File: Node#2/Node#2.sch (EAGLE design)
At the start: 75 parts, among them IC1 TSL25911FN, J1 68712414522, Q2 SI1308EDL-T1-GE3, U2 RV8564C3, U4 TPS63001DRCT

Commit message: Node#2 sorted, Node#1 small adjusts
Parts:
- added R2: 100, rcl:R-EU_R0805
- added U$9: BZB984, BlueHome:BZB984
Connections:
- new net N$2: D2.A, R2.1
- net +3V3: no longer D2.A
- net +3V3_RTC: now also U$9.2
- net GND: now also U$9.3
- net V+: now also R2.2

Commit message: Schematic finished (hopefully) !
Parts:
- added C34: (no value), rcl:C-EUC0805
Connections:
- removed net N$26: C31.2, C33.2, MK1.VDD
- net +3V3: now also MK1.VDD
- net +5V: no longer U$1.2
- net ADC2: now also C34.1
- net GND: now also C31.2, C33.2, C34.2
- net V+: now also U$1.2
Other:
- note added: "E-Ink Display"
- note added: "Power"
- note added: "Sensors & LEDs"

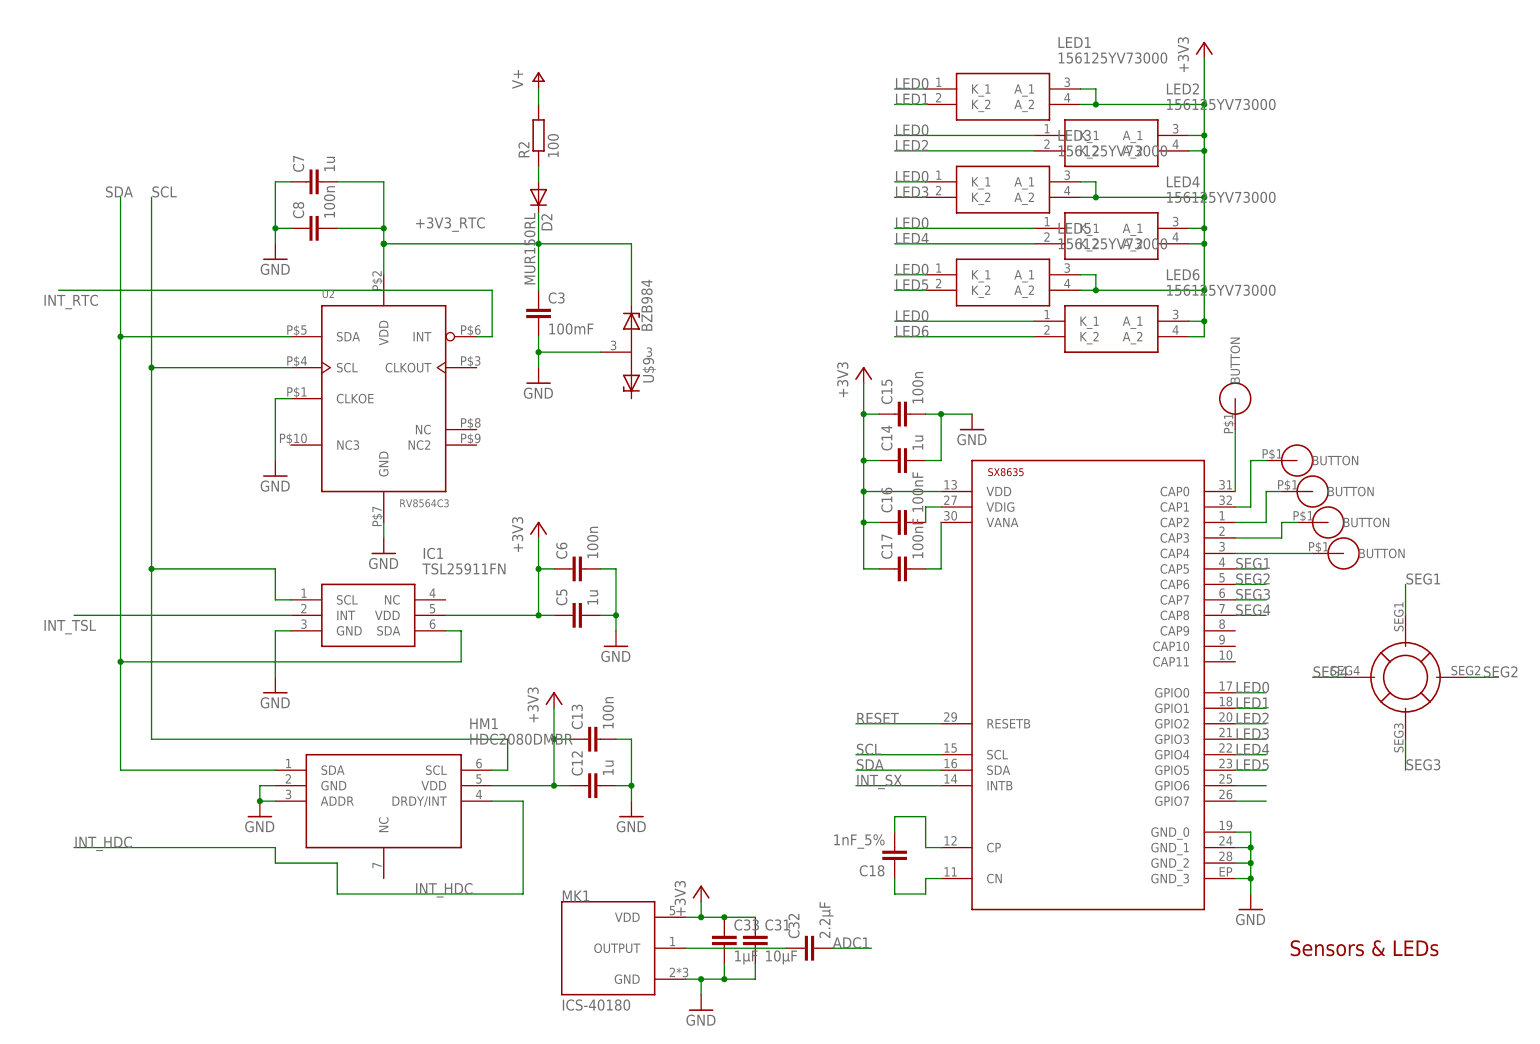
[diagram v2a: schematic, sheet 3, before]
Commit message: Changed Packages, connected GPIO
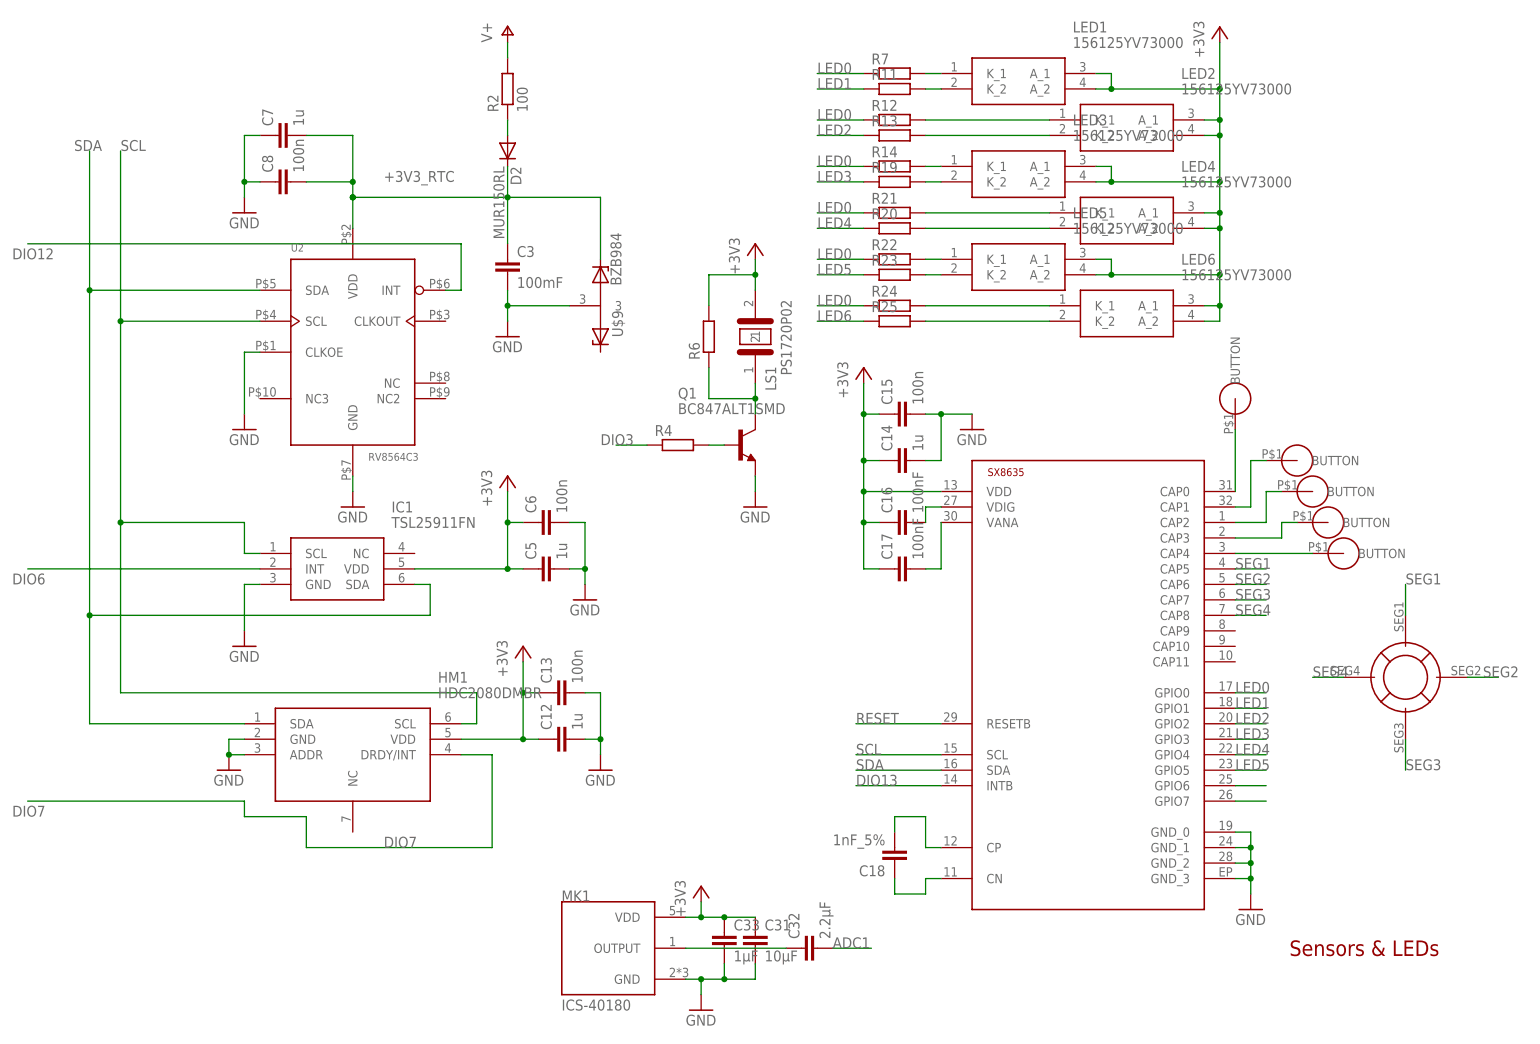
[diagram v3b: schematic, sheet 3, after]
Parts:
- added LS1: PS1720P02, BlueHome:PS1720P02
- added Q1: BC847ALT1SMD, transistor-npn:BC847ALT1SMD
- added R11, R12, R13, R14, R19, R20, R21, R22, R23, R24, R25, R4, R6, R7: (no value), rcl:R-EU_R0805
- L1: device rcl:L-EUL4532P -> rcl:L-EUL5038P
- L2: device rcl:L-EUL1812 -> rcl:L-EUL5038P
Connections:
- net INT_HDC renamed DIO7
- net INT_RTC renamed DIO12
- net INT_SX renamed DIO13
- net INT_TSL renamed DIO6
- new net DIO0: J1.13
- new net DIO1: J1.12
- new net DIO2: J1.14
- new net DIO3: R4.1
- new net N$13: LED3.K_2, R19.2
- new net N$16: LED5.K_1, R22.2
- new net N$17: LED5.K_2, R23.2
- new net N$25: LED2.K_1, R12.2
- new net N$26: LED2.K_2, R13.2
- new net N$27: LED4.K_1, R21.2
- new net N$3: LS1.1, Q1.C, R6.1
- new net N$30: LED4.K_2, R20.2
- new net N$36: LED6.K_1, R24.2
- new net N$37: LED6.K_2, R25.2
- new net N$4: LED1.K_1, R7.2
- new net N$5: LED1.K_2, R11.2
- new net N$6: Q1.B, R4.2
- new net N$7: LED3.K_1, R14.2
- net +3V3: now also LS1.2, R6.2
- net CS: no longer J1.12
- net GND: now also Q1.E
- net LED0: now also R12.1, R14.1, R21.1, R22.1, R24.1, R7.1; no longer LED1.K_1, LED2.K_1, LED3.K_1, LED4.K_1, LED5.K_1, LED6.K_1
- net LED1: now also R11.1; no longer LED1.K_2
- net LED2: now also R13.1; no longer LED2.K_2
- net LED3: now also R19.1; no longer LED3.K_2
- net LED4: now also R20.1; no longer LED4.K_2
- net LED5: now also R23.1; no longer LED5.K_2
- net LED6: now also R25.1; no longer LED6.K_2
- net MOSI: no longer J1.14
- net SCLK: no longer J1.13
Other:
- moved on the sheet: C12, C13, C3, C5, C6, C7, C8, D2, HM1, IC1, LED1, LED2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

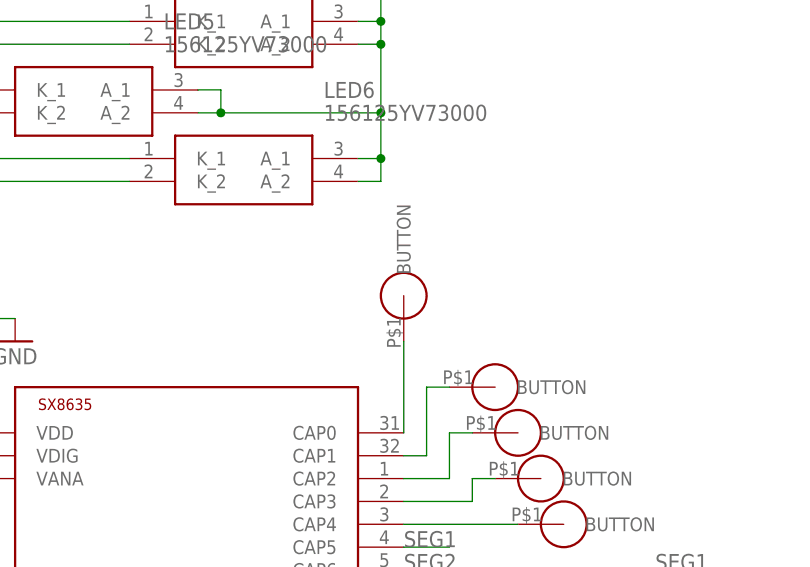
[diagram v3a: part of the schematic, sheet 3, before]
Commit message: Created node#2 Layout and Proximity Sensor in Library
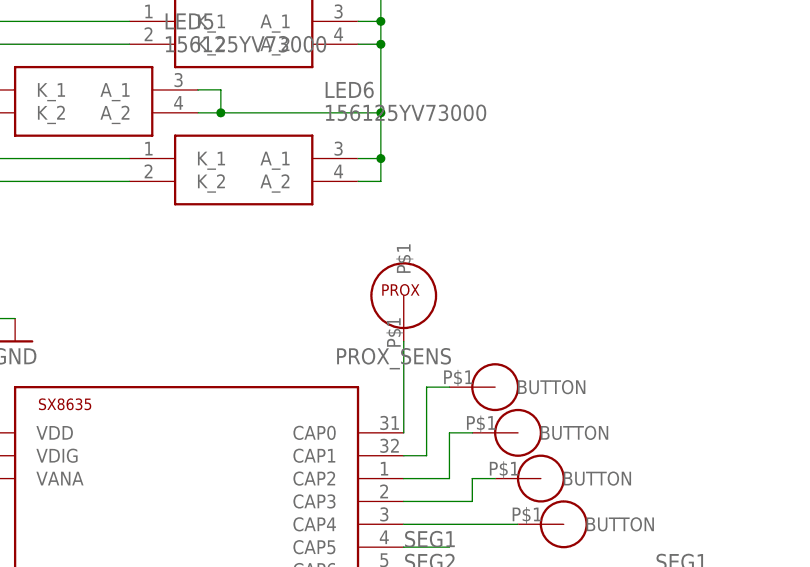
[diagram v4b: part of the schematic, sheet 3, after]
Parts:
- U$7: value TOUCH_BUTTON -> PROXIMITY; device BlueHome:TOUCH_BUTTON -> BlueHome:PROXIMITY
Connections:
- removed net +5V: R5.2
- removed net N$33: U$2.CAP0, U$7.BUTTON
- new net PROX_SENS: U$2.CAP0, U$7.P$1
- net V+: now also R5.2
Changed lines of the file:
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@@
 <grid distance="0.1" unitdist="inch" unit="inch" style="lines" multiple="1" display="no" altdistance="0.01" altunitdist="inch" altunit="inch"/>
 <layers>
-<layer number="1" name="Top" color="4" fill="1" visible="yes" active="no"/>
-<layer number="2" name="Route2" color="1" fill="3" visible="yes" active="no"/>
-<layer number="3" name="Route3" color="4" fill="3" visible="yes" active="no"/>
-<layer number="4" name="Route4" color="1" fill="4" visible="yes" active="no"/>
-<layer number="5" name="Route5" color="4" fill="4" visible="yes" active="no"/>
-<layer number="6" name="Route6" color="1" fill="8" visible="yes" active="no"/>
-<layer number="7" name="Route7" color="4" fill="8" visible="yes" active="no"/>
-<layer number="8" name="Route8" color="1" fill="2" visible="yes" active="no"/>
-<layer number="9" name="Route9" color="4" fill="2" visible="yes" active="no"/>
-<layer number="10" name="Route10" color="1" fill="7" visible="yes" active="no"/>
-<layer number="11" name="Route11" color="4" fill="7" visible="yes" active="no"/>
-<layer number="12" name="Route12" color="1" fill="5" visible="yes" active="no"/>
-<layer number="13" name="Route13" color="4" fill="5" visible="yes" active="no"/>
-<layer number="14" name="Route14" color="1" fill="6" visible="yes" active="no"/>
-<layer number="15" name="Route15" color="4" fill="6" visible="yes" active="no"/>
-<layer number="16" name="Bottom" color="1" fill="1" visible="yes" active="no"/>
-<layer number="17" name="Pads" color="2" fill="1" visible="yes" active="no"/>
-<layer number="18" name="Vias" color="2" fill="1" visible="yes" active="no"/>
-<layer number="19" name="Unrouted" color="6" fill="1" visible="yes" active="no"/>
-<layer number="20" name="Dimension" color="15" fill="1" visible="yes" active="no"/>
-<layer number="21" name="tPlace" color="7" fill="1" visible="yes" active="no"/>
-<layer number="22" name="bPlace" color="7" fill="1" visible="yes" active="no"/>
-<layer number="23" name="tOrigins" color="15" fill="1" visible="yes" active="no"/>
-<layer number="24" name="bOrigins" color="15" fill="1" visible="yes" active="no"/>
-<layer number="25" name="tNames" color="7" fill="1" visible="yes" active="no"/>
-<layer number="26" name="bNames" color="7" fill="1" visible="yes" active="no"/>
-<layer number="27" name="tValues" color="7" fill="1" visible="yes" active="no"/>
-<layer number="28" name="bValues" color="7" fill="1" visible="yes" active="no"/>
+<layer number="1" name="Top" color="4" fill="1" visible="no" active="no"/>
+<layer number="2" name="Route2" color="1" fill="3" visible="no" active="no"/>
+<layer number="3" name="Route3" color="4" fill="3" visible="no" active="no"/>
+<layer number="4" name="Route4" color="1" fill="4" visible="no" active="no"/>
+<layer number="5" name="Route5" color="4" fill="4" visible="no" active="no"/>
+<layer number="6" name="Route6" color="1" fill="8" visible="no" active="no"/>
+<layer number="7" name="Route7" color="4" fill="8" visible="no" active="no"/>
+<layer number="8" name="Route8" color="1" fill="2" visible="no" active="no"/>
+<layer number="9" name="Route9" color="4" fill="2" visible="no" active="no"/>
+<layer number="10" name="Route10" color="1" fill="7" visible="no" active="no"/>
+<layer number="11" name="Route11" color="4" fill="7" visible="no" active="no"/>
+<layer number="12" name="Route12" color="1" fill="5" visible="no" active="no"/>
+<layer number="13" name="Route13" color="4" fill="5" visible="no" active="no"/>
+<layer number="14" name="Route14" color="1" fill="6" visible="no" active="no"/>
+<layer number="15" name="Route15" color="4" fill="6" visible="no" active="no"/>
+<layer number="16" name="Bottom" color="1" fill="1" visible="no" active="no"/>
+<layer number="17" name="Pads" color="2" fill="1" visible="no" active="no"/>
+<layer number="18" name="Vias" color="2" fill="1" visible="no" active="no"/>
+<layer number="19" name="Unrouted" color="6" fill="1" visible="no" active="no"/>
+<layer number="20" name="Dimension" color="15" fill="1" visible="no" active="no"/>
+<layer number="21" name="tPlace" color="7" fill="1" visible="no" active="no"/>
+<layer number="22" name="bPlace" color="7" fill="1" visible="no" active="no"/>
+<layer number="23" name="tOrigins" color="15" fill="1" visible="no" active="no"/>
+<layer number="24" name="bOrigins" color="15" fill="1" visible="no" active="no"/>
+<layer number="25" name="tNames" color="7" fill="1" visible="no" active="no"/>
+<layer number="26" name="bNames" color="7" fill="1" visible="no" active="no"/>
+<layer number="27" name="tValues" color="7" fill="1" visible="no" active="no"/>
+<layer number="28" name="bValues" color="7" fill="1" visible="no" active="no"/>
 <layer number="29" name="tStop" color="7" fill="3" visible="no" active="no"/>
 <layer number="30" name="bStop" color="7" fill="6" visible="no" active="no"/>
@@
 <layer number="35" name="tGlue" color="7" fill="4" visible="no" active="no"/>
 <layer number="36" name="bGlue" color="7" fill="5" visible="no" active="no"/>
-<layer number="37" name="tTest" color="7" fill="1" visible="yes" active="no"/>
-<layer number="38" name="bTest" color="7" fill="1" visible="yes" active="no"/>
+<layer number="37" name="tTest" color="7" fill="1" visible="no" active="no"/>
+<layer number="38" name="bTest" color="7" fill="1" visible="no" active="no"/>
 <layer number="39" name="tKeepout" color="4" fill="11" visible="no" active="no"/>
 <layer number="40" name="bKeepout" color="1" fill="11" visible="no" active="no"/>
@@
 <layer number="44" name="Drills" color="7" fill="1" visible="no" active="no"/>
 <layer number="45" name="Holes" color="7" fill="1" visible="no" active="no"/>
-<layer number="46" name="Milling" color="3" fill="1" visible="yes" active="no"/>
-<layer number="47" name="Measures" color="7" fill="1" visible="yes" active="no"/>
-<layer number="48" name="Document" color="7" fill="1" visible="yes" active="no"/>
-<layer number="49" name="Reference" color="7" fill="1" visible="yes" active="no"/>
-<layer number="51" name="tDocu" color="7" fill="1" visible="yes" active="no"/>
-<layer number="52" name="bDocu" color="7" fill="1" visible="yes" active="no"/>
+<layer number="46" name="Milling" color="3" fill="1" visible="no" active="no"/>
+<layer number="47" name="Measures" color="7" fill="1" visible="no" active="no"/>
+<layer number="48" name="Document" color="7" fill="1" visible="no" active="no"/>
+<layer number="49" name="Reference" color="7" fill="1" visible="no" active="no"/>
+<layer number="51" name="tDocu" color="7" fill="1" visible="no" active="no"/>
+<layer number="52" name="bDocu" color="7" fill="1" visible="no" active="no"/>
 <layer number="90" name="Modules" color="5" fill="1" visible="yes" active="yes"/>
 <layer number="91" name="Nets" color="2" fill="1" visible="yes" active="yes"/>
@@
 <part name="U$5" library="BlueHome" deviceset="TOUCH_BUTTON" device=""/>
 <part name="U$6" library="BlueHome" deviceset="TOUCH_BUTTON" device=""/>
-<part name="U$7" library="BlueHome" deviceset="TOUCH_BUTTON" device=""/>
 <part name="U$8" library="BlueHome" deviceset="WHEEL" device=""/>
 <part name="GND19" library="supply1" deviceset="GND" device=""/>
@@
 <part name="R24" library="rcl" library_urn="urn:adsk.eagle:library:334" deviceset="R-EU_" device="R0805" package3d_urn="urn:adsk.eagle:package:23553/2"/>
 <part name="R25" library="rcl" library_urn="urn:adsk.eagle:library:334" deviceset="R-EU_" device="R0805" package3d_urn="urn:adsk.eagle:package:23553/2"/>
+<part name="U$7" library="BlueHome" deviceset="PROXIMITY" device=""/>
 </parts>
 <sheets>
@@
 </segment>
 </net>
-<net name="+5V" class="0">
-<segment>
-<pinref part="P+3" gate="1" pin="V+"/>
-<wire x1="31.75" y1="74.93" x2="31.75" y2="69.85" width="0.1524" layer="91"/>
-<pinref part="R5" gate="G$1" pin="2"/>
-</segment>
-</net>
 <net name="N$9" class="0">
 <segment>
@@
 <pinref part="U$1" gate="A" pin="2"/>
 <wire x1="106.68" y1="132.08" x2="99.06" y2="132.08" width="0.1524" layer="91"/>
+</segment>
+<segment>
+<pinref part="R5" gate="G$1" pin="2"/>
+<pinref part="P+3" gate="1" pin="V+"/>
+<wire x1="31.75" y1="69.85" x2="31.75" y2="74.93" width="0.1524" layer="91"/>
 </segment>
 </net>
@@
 <instance part="U$5" gate="G$1" x="223.52" y="91.44" smashed="yes" rot="R180"/>
 <instance part="U$6" gate="G$1" x="226.06" y="86.36" smashed="yes" rot="R180"/>
-<instance part="U$7" gate="G$1" x="208.28" y="111.76" smashed="yes" rot="R270"/>
 <instance part="U$8" gate="G$1" x="236.22" y="66.04" smashed="yes"/>
 <instance part="GND19" gate="1" x="45.72" y="106.68" smashed="yes">
@@
 <attribute name="VALUE" x="148.59" y="121.158" size="1.778" layer="96"/>
 </instance>
+<instance part="U$7" gate="G$1" x="208.28" y="111.76" smashed="yes"/>
 </instances>
 <busses>
@@
 </segment>
 </net>
-<net name="N$33" class="0">
+<net name="PROX_SENS" class="0">
 <segment>
 <pinref part="U$2" gate="G$1" pin="CAP0"/>
 <wire x1="208.28" y1="96.52" x2="208.28" y2="106.68" width="0.1524" layer="91"/>
-<pinref part="U$7" gate="G$1" pin="BUTTON"/>
-</segment>
-</net>
+<pinref part="U$7" gate="G$1" pin="P$1"/>
+<label x="200.66" y="104.14" size="1.778" layer="95"/>
+</segment>
+</net>

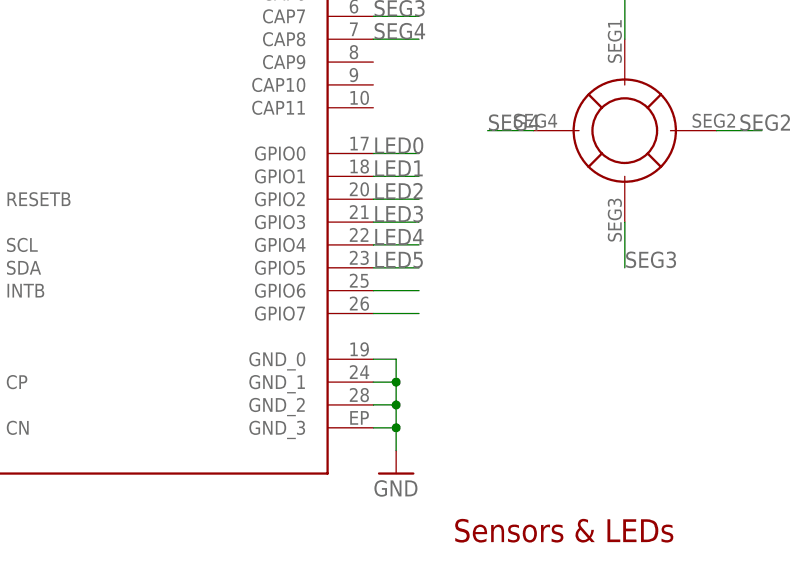
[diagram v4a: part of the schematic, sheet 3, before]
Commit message: Worked on Layout on Node#2
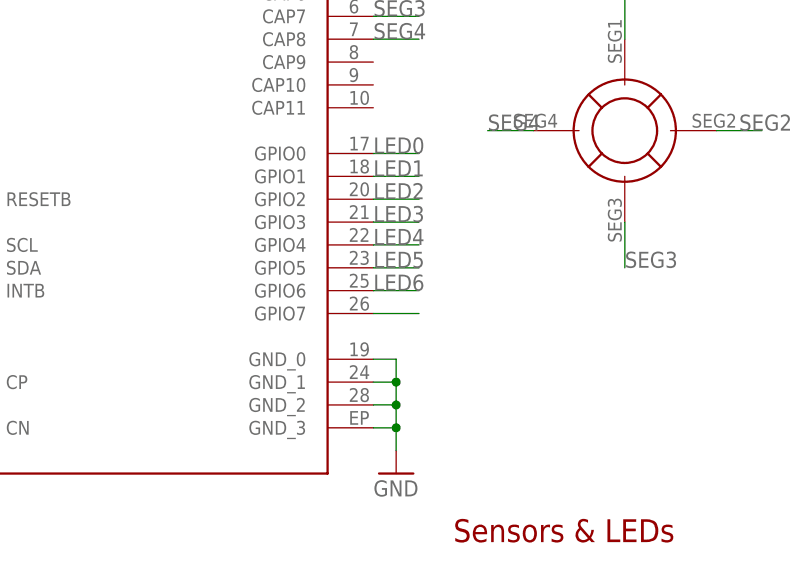
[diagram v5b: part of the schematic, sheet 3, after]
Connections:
- removed net N$34: U$2.GPIO6
- net LED6: now also U$2.GPIO6
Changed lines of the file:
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@@
-</segment>
-</net>
-<net name="N$34" class="0">
-<segment>
-<pinref part="U$2" gate="G$1" pin="GPIO6"/>
-<wire x1="208.28" y1="48.26" x2="213.36" y2="48.26" width="0.1524" layer="91"/>
 </segment>
 </net>
@@
 <pinref part="R25" gate="G$1" pin="1"/>
 </segment>
+<segment>
+<pinref part="U$2" gate="G$1" pin="GPIO6"/>
+<wire x1="208.28" y1="48.26" x2="213.36" y2="48.26" width="0.1524" layer="91"/>
+<label x="208.28" y="48.26" size="1.778" layer="95"/>
+</segment>
 </net>
